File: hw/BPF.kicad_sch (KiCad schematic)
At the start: 13 parts

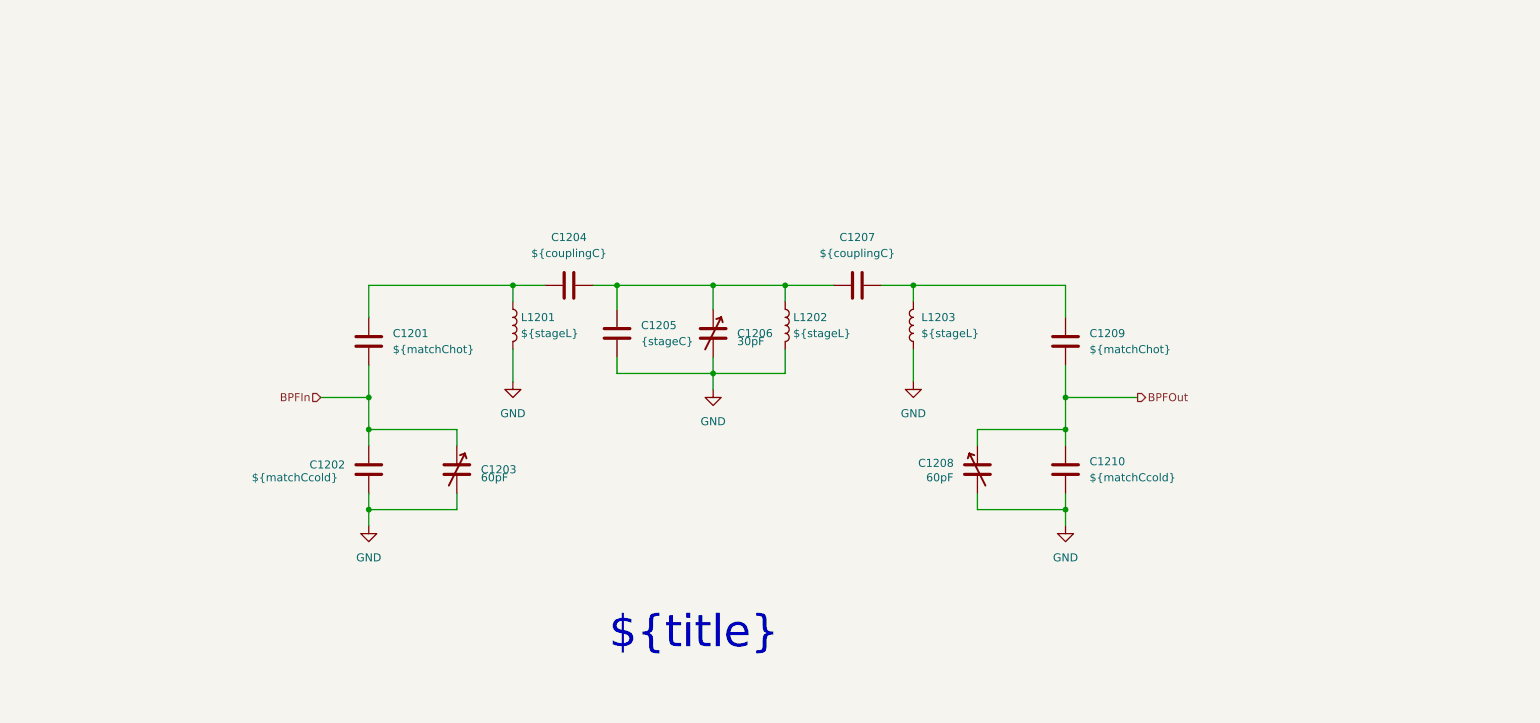
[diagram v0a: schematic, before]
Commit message: Starting to build BPFs for 7 bands
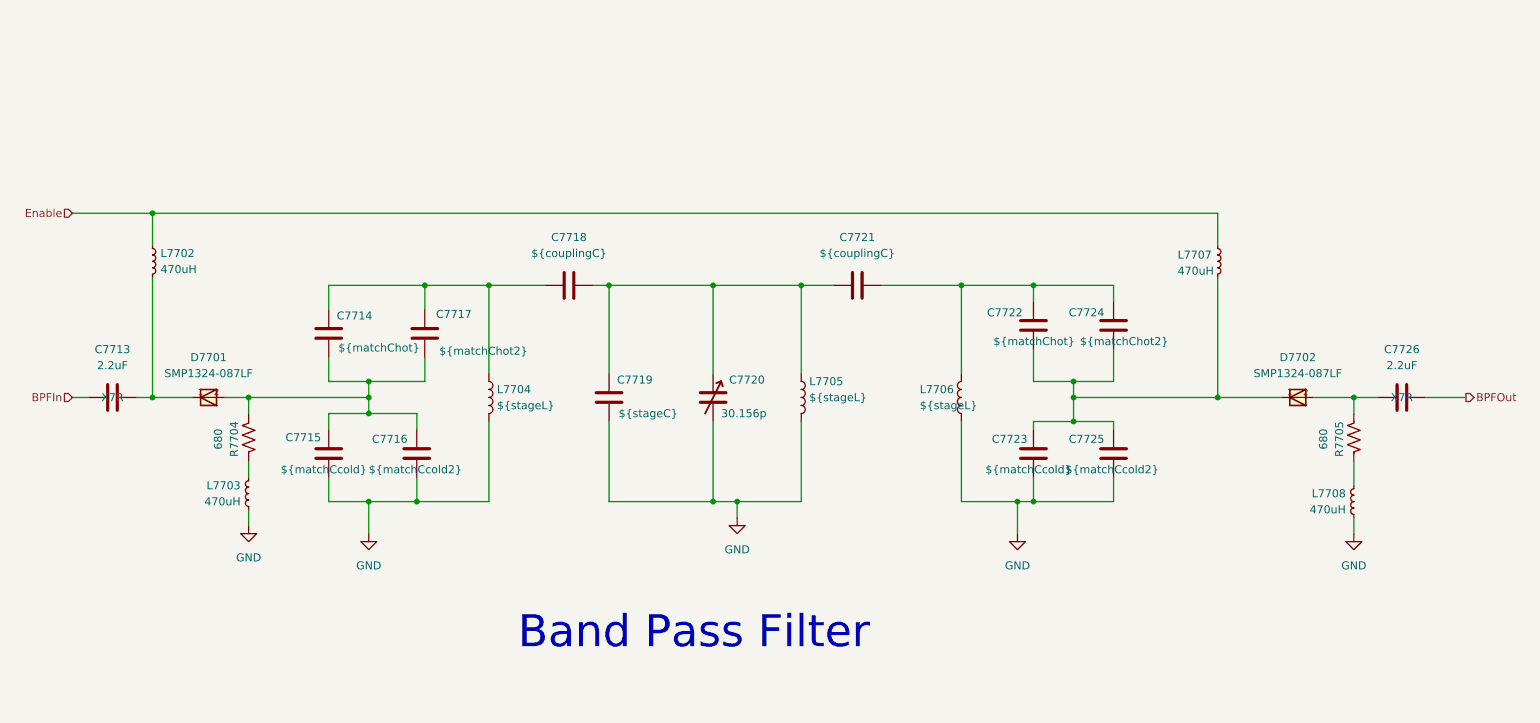
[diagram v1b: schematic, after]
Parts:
- removed C1203, C1208: 60pF, PCM_Capacitor_THT_AKL:C_Trimmer_BFC2-808_L7.3mm_W5.5mm_P5.6mm_Hole, symbol PCM_Capacitor_AKL:C_Trim_Vishay_BFC2-808_D7.5mm_Hole
- removed C1210: ${matchCcold}, symbol Device:C
- added C7713, C7726: 2.2uF, symbol Device:C
- added C7716, C7725: ${matchCcold2}, symbol Device:C
- added C7717: ${matchChot2}, symbol Device:C
- added C7722: ${matchChot}, symbol Device:C
- added C7723: ${matchCcold}, symbol Device:C
- added D7701, D7702: SMP1324-087LF, SMP1324-087LF:QFN2, symbol SMP1324-087LF:SMP1324-087LF
- added L7702, L7703, L7707, L7708: 470uH, symbol Device:L_Small
- added R7704, R7705: 680, symbol Device:R_US
- C7715: renamed from C1202; footprint 220pF -> (none)
- C7719: renamed from C1205; value {stageC} -> ${stageC}
- C7720: renamed from C1206; value 30pF -> 30.156p
- C7724: renamed from C1209; value ${matchChot} -> ${matchChot2}
- renumbered C1201 to C7714, C1204 to C7718, C1207 to C7721, L1201 to L7704, L1202 to L7705, L1203 to L7706
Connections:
- net BPFIn: now also C7713.1; no longer C7714.2, C7715.1
- net BPFOut: now also C7726.2; no longer C7724.2
- net GND: now also C7716.2, C7723.2, C7725.2, L7703.2, L7708.2
- net at C7714.1, C7718.1, L7704.1: now also C7717.1
- net at C7721.2, C7724.1, L7706.1: now also C7722.1
- new net: C7722.2, C7723.1, C7724.2, C7725.1, D7702.1, L7707.2
- new net: L7703.1, R7704.1
- new net: C7714.2, C7715.1, C7716.1, C7717.2, D7701.2, R7704.2
- new net: C7713.2, D7701.1, L7702.2
- new net: L7708.1, R7705.1
- new net: C7726.1, D7702.2, R7705.2
- new net Enable: L7702.1, L7707.1
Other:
- title: ${title} -> Band Pass Filter
- moved on the sheet: C7714, C7715, C7719, C7720, C7724, L7704, L7705, L7706

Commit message: Filter calc checkpoint
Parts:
- C7713, C7726: value 2.2uF -> 0.1uF; cap-type X7R -> NP0
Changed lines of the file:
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@@
 			)
 		)
-		(property "Sim.Library" "/home/alan/ham/USB-SSB-txcvr/spice-models/rn242sm_SPICE.lib"
+		(property "Sim.Library" "/home/alan/ham/usb-ssb-txcvr/spice-models/rn242sm_SPICE.lib"
 			(at 44.45 80.01 0)
 			(effects
@@
 			)
 		)
-		(property "Value" "2.2uF"
+		(property "Value" "0.1uF"
 			(at 233.68 74.93 90)
 			(effects
@@
 			)
 		)
-		(property "cap-type" "X7R"
+		(property "cap-type" "NP0"
 			(at 233.68 80.01 90)
+			(effects
+				(font
+					(size 1.27 1.27)
+				)
+			)
+		)
+		(property "r-power" ""
+			(at 233.68 80.01 0)
 			(effects
 				(font
@@
 			)
 		)
-		(property "Value" "2.2uF"
+		(property "Value" "0.1uF"
 			(at 29.21 74.93 90)
 			(effects
@@
 			)
 		)
-		(property "cap-type" "X7R"
+		(property "cap-type" "NP0"
 			(at 29.21 80.01 90)
+			(effects
+				(font
+					(size 1.27 1.27)
+				)
+			)
+		)
+		(property "r-power" ""
+			(at 29.21 80.01 0)
 			(effects
 				(font
@@
 			)
 		)
-		(property "Sim.Library" "/home/alan/ham/USB-SSB-txcvr/spice-models/rn242sm_SPICE.lib"
+		(property "Sim.Library" "/home/alan/ham/usb-ssb-txcvr/spice-models/rn242sm_SPICE.lib"
 			(at 217.17 80.01 0)
 			(effects

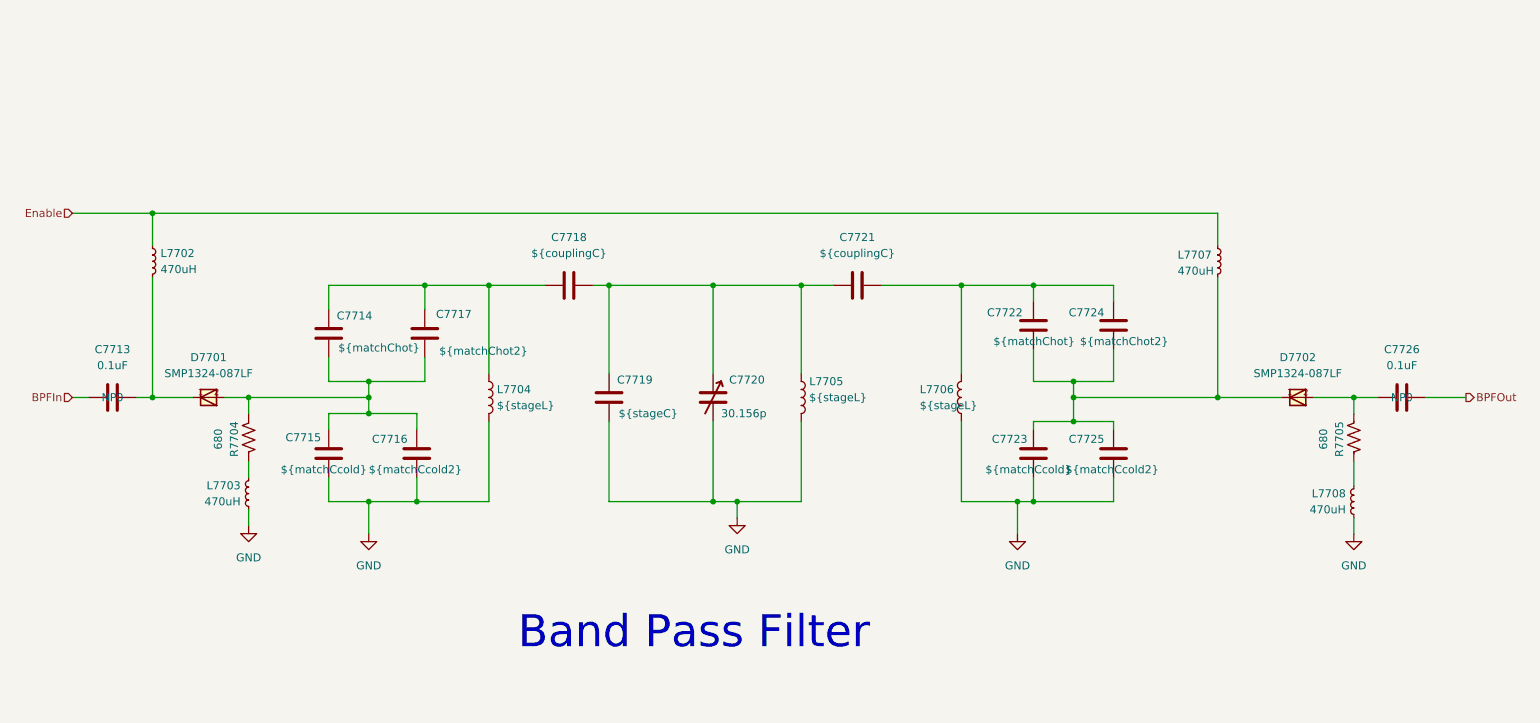
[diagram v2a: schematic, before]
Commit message: Getting closer to having all (ten) BPFs designed. Maybe I can try some layout next.
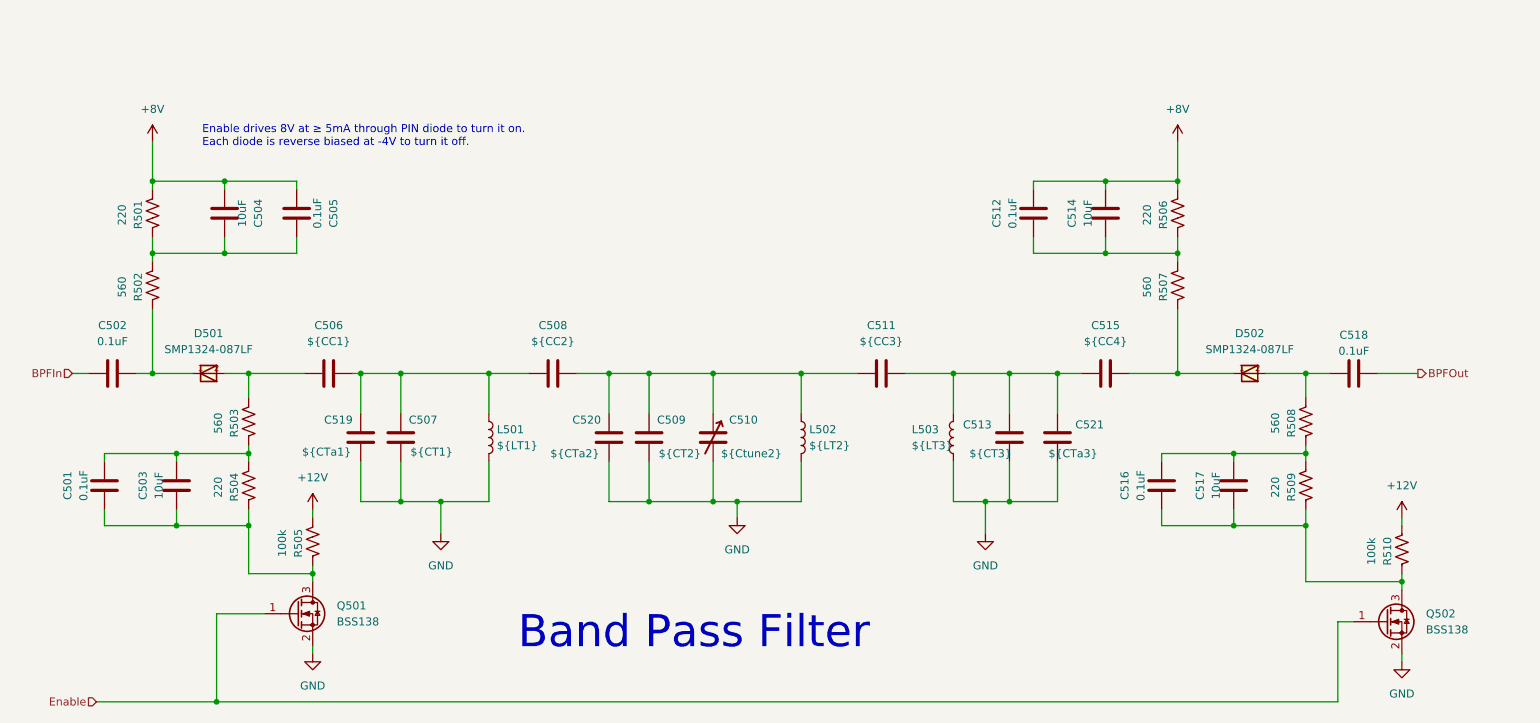
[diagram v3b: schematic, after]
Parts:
- removed C7715, C7723: ${matchCcold}, symbol Device:C
- removed C7716, C7725: ${matchCcold2}, symbol Device:C
- removed C7717, C7724: ${matchChot2}, symbol Device:C
- removed L7702, L7703, L7707, L7708: 470uH, symbol Device:L_Small
- removed R7705: 680, symbol Device:R_US
- added C501, C505, C512, C516: 0.1uF, symbol Device:C
- added C503, C504, C514, C517: 10uF, symbol Device:C
- added C506: ${CC1}, symbol Device:C
- added C515: ${CC4}, symbol Device:C
- added C519: ${CTa1}, symbol Device:C
- added C520: ${CTa2}, symbol Device:C
- added C521: ${CTa3}, symbol Device:C
- added Q501, Q502: BSS138, Package_TO_SOT_SMD:SOT-23, symbol Transistor_FET:BSS138
- added R501, R504, R506, R509: 220, symbol Device:R_US
- added R502, R507, R508: 560, symbol Device:R_US
- added R505, R510: 100k, symbol Device:R_US
- C502: renamed from C7713; cap-type NP0 -> (none)
- C507: renamed from C7714; value ${matchChot} -> ${CT1}
- C508: renamed from C7718; value ${couplingC} -> ${CC2}
- C509: renamed from C7719; value ${stageC} -> ${CT2}
- C510: renamed from C7720; value 30.156p -> ${Ctune2}
- C511: renamed from C7721; value ${couplingC} -> ${CC3}
- C513: renamed from C7722; value ${matchChot} -> ${CT3}
- C518: renamed from C7726; cap-type NP0 -> (none)
- L501: renamed from L7704; value ${stageL} -> ${LT1}
- L502: renamed from L7705; value ${stageL} -> ${LT2}
- L503: renamed from L7706; value ${stageL} -> ${LT3}
- R503: renamed from R7704; value 680 -> 560
- renumbered D7701 to D501, D7702 to D502
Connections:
- net Enable: now also Q501.1 (G), Q502.1 (G)
- net GND: now also C507.2, C513.2, C519.2, C520.2, C521.2, Q501.2 (S), Q502.2 (S)
- net at C511.2, C513.1, L503.1: now also C515.1, C521.1
- net at D502.1: now also C515.2, R507.1; no longer C513.2
- net at C507.1, C508.1, L501.1: now also C506.2, C519.1
- net at C508.2, C509.1, C510.1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: now also C520.1
- net at R503.1: now also C501.2, C503.2, R504.2
- net at D501.2, R503.2: now also C506.1; no longer C507.2
- net at C502.2, D501.1: now also R502.1
- net at C518.1, D502.2: now also R508.2
- new net: C516.1, C517.1, Q502.3 (D), R509.1, R510.1
- new net: C516.2, C517.2, R508.1, R509.2
- new net: C501.1, C503.1, Q501.3 (D), R504.1, R505.1
- new net: C504.1, C505.1, R501.1, R502.2
- new net: C512.1, C514.1, R506.1, R507.2
- new net +12V: R505.2, R510.2
- new net +8V: C504.2, C505.2, C512.2, C514.2, R501.2, R506.2
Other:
- note added: "Enable drives 8V at ≥ 5mA through PIN diode to turn it on. Each diode is reverse biased at -4V to turn it off."
- moved on the sheet: C502, C507, C508, C509, C510, C511, C513, C518, D501, D502, L501, L502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

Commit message: Checkpoint hardware. Add README with some notes about software services we need to create.
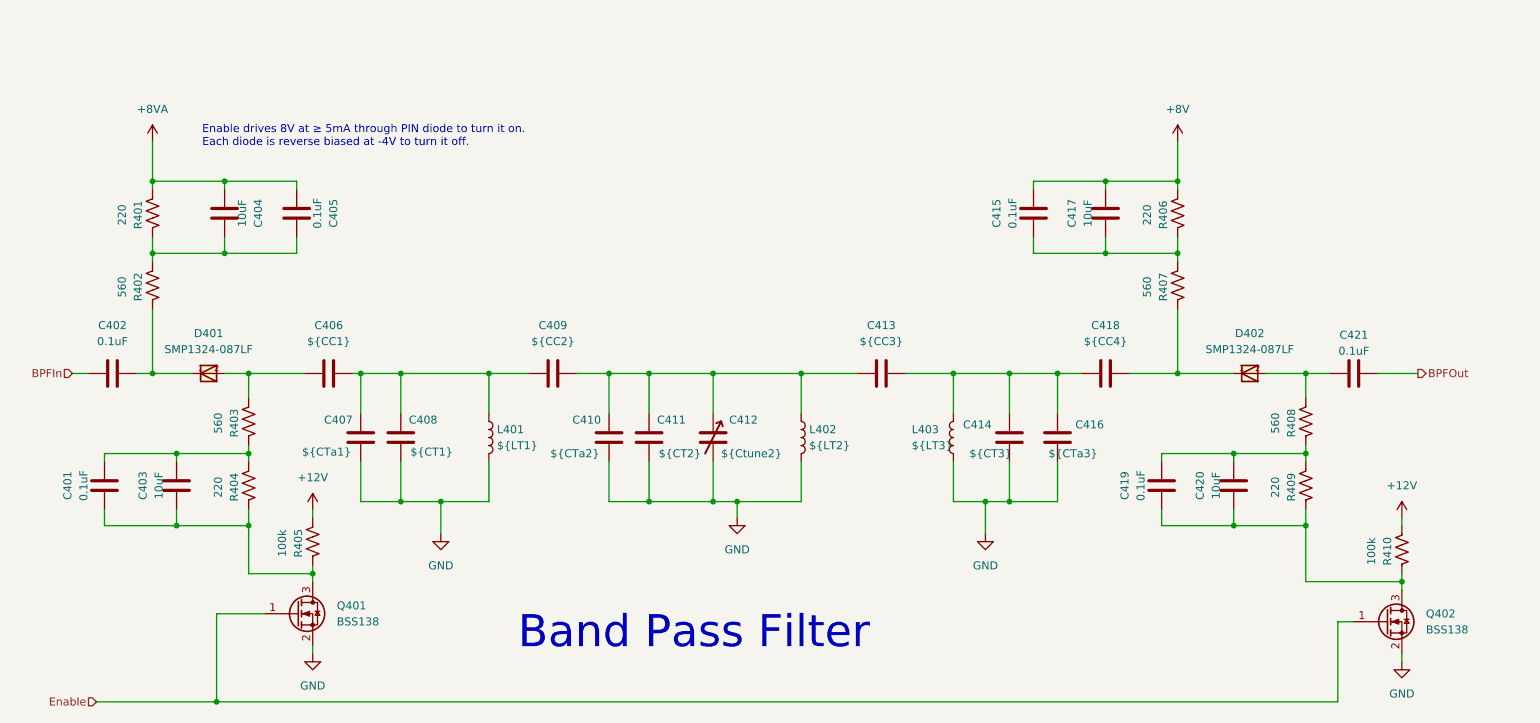
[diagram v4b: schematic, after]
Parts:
- renumbered C501 to C401, C502 to C402, C503 to C403, C504 to C404, C505 to C405, C506 to C406, C519 to C407, C507 to C408, C508 to C409, C520 to C410, C509 to C411, C510 to C412, C511 to C413, C513 to C414, C512 to C415, C521 to C416, C514 to C417, C515 to C418, C516 to C419, C517 to C420, C518 to C421, D501 to D401, D502 to D402, L501 to L401, L502 to L402, L503 to L403, Q501 to Q401, Q502 to Q402, R501 to R401, R502 to R402, R503 to R403, R504 to R404, R505 to R405, R506 to R406, R507 to R407, R508 to R408, R509 to R409, R510 to R410
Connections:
- net +8V: no longer C404.2, C405.2, R401.2
- new net +8VA: C404.2, C405.2, R401.2

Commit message: Add NOTES for summarizing the transmitter architecture. Starting to work on PIN switches more intently, and building a simulation model for the EER buck regulator and FPGA NCO phase modulator.
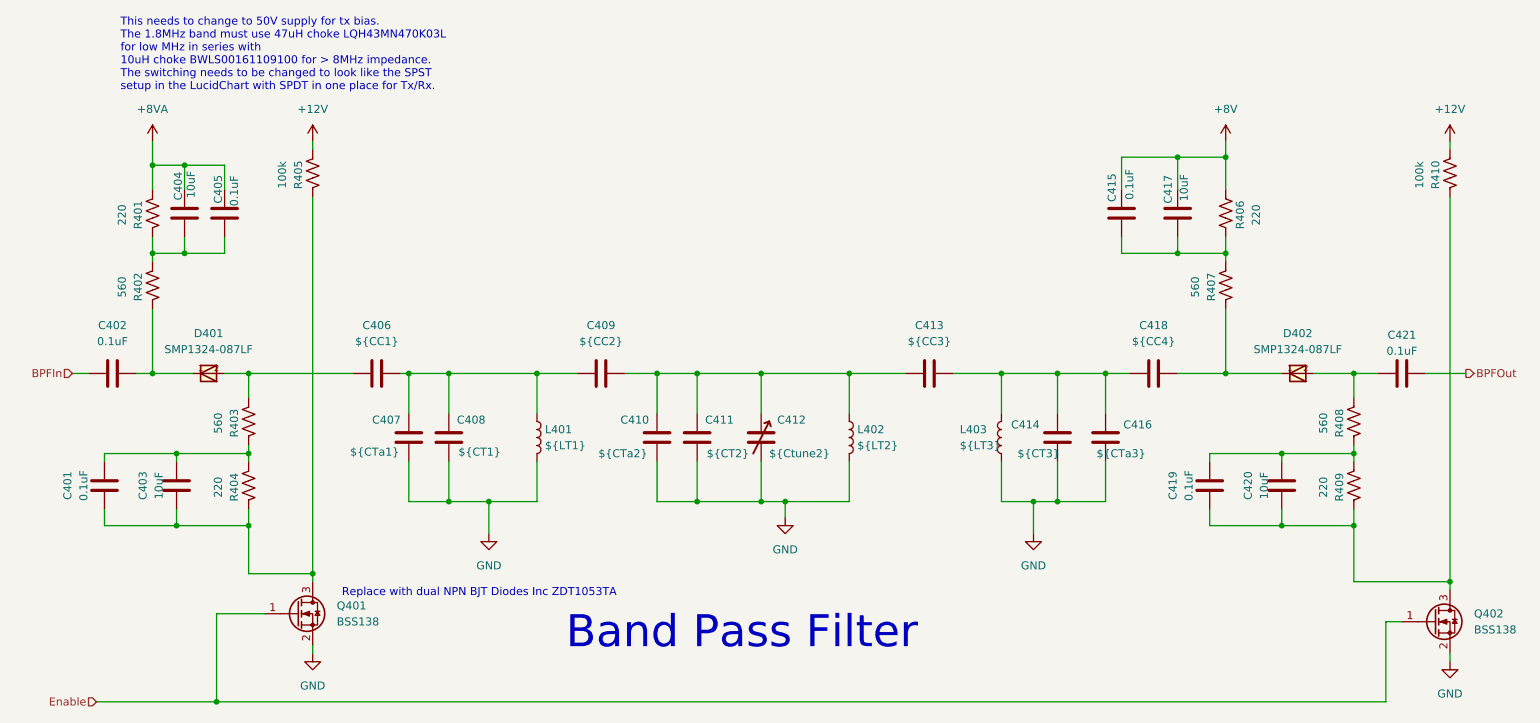
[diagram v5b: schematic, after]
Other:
- note added: "Replace with dual NPN BJT Diodes Inc ZDT1053TA"
- note added: "This needs to change to 50V supply for tx bias. The 1.8MHz band must use 47uH choke LQH43MN470K03L for low MHz in series with 10uH choke BWLS00161109100 for > 8MHz impedance. The switching needs to be changed to look like the SPST setup in the LucidChart with SPDT in one place for Tx/Rx."
- note removed: "Enable drives 8V at ≥ 5mA through PIN diode to turn it on. Each diode is reverse biased at -4V to turn it off."
- moved on the sheet: C404, C405, C406, C407, C408, C409, C410, C411, C412, C413, C414, C415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
